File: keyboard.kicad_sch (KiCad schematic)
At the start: 8 parts, among them J3 KEYBOARD / USER FIT, J5 MODULE LINK / OPTIONAL, U8 PCF8574T

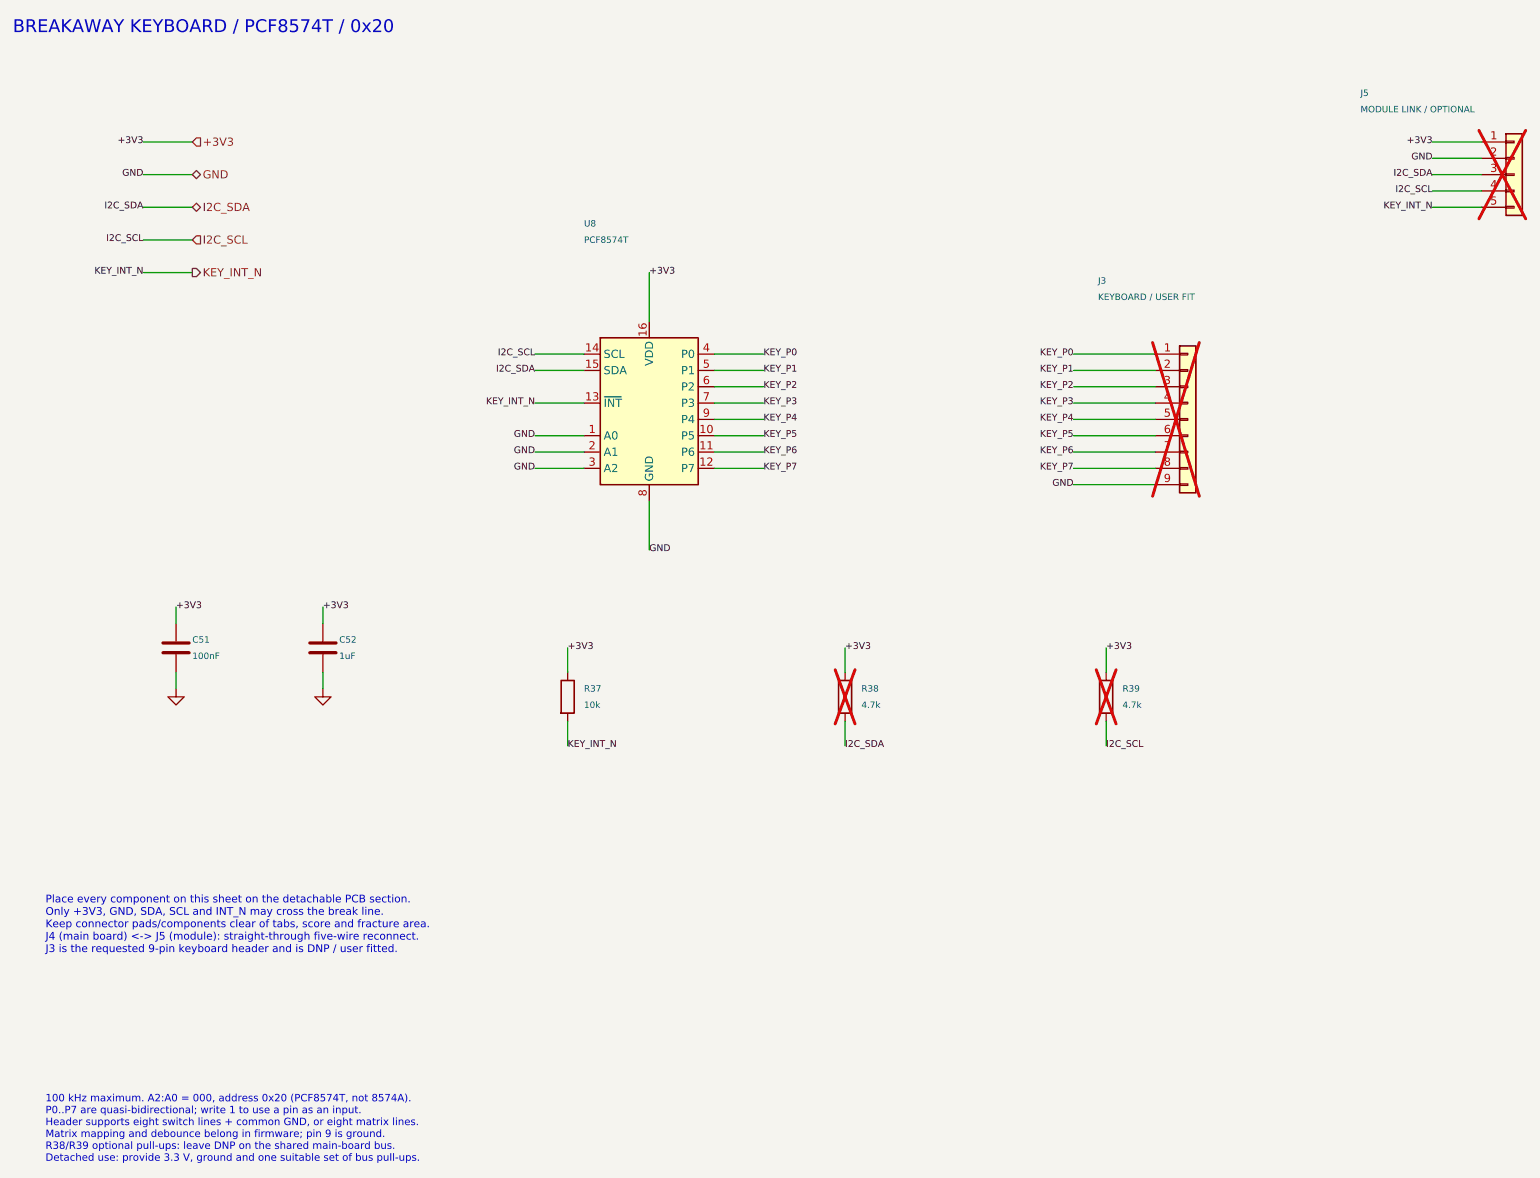
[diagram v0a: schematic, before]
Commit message: Keep keypad signals on center seven header pins
Retain the DNP nine-pin header with pins 1 and 9 isolated. Map pins 2-8
to PCF8574 P0-P6, preserving the early prototype's seven-contact order,
and leave P7 unconnected.

Document the researched keypad matrix mapping and scanning behavior.
Update schematic notes, connectivity checks, BOM, verification report,
and schematic PDF.

Validation: zero native KiCad ERC violations; seven-contact mapping
matches the early netlist; isolated pins and DNP status verified;
updated schematic pages visually inspected.
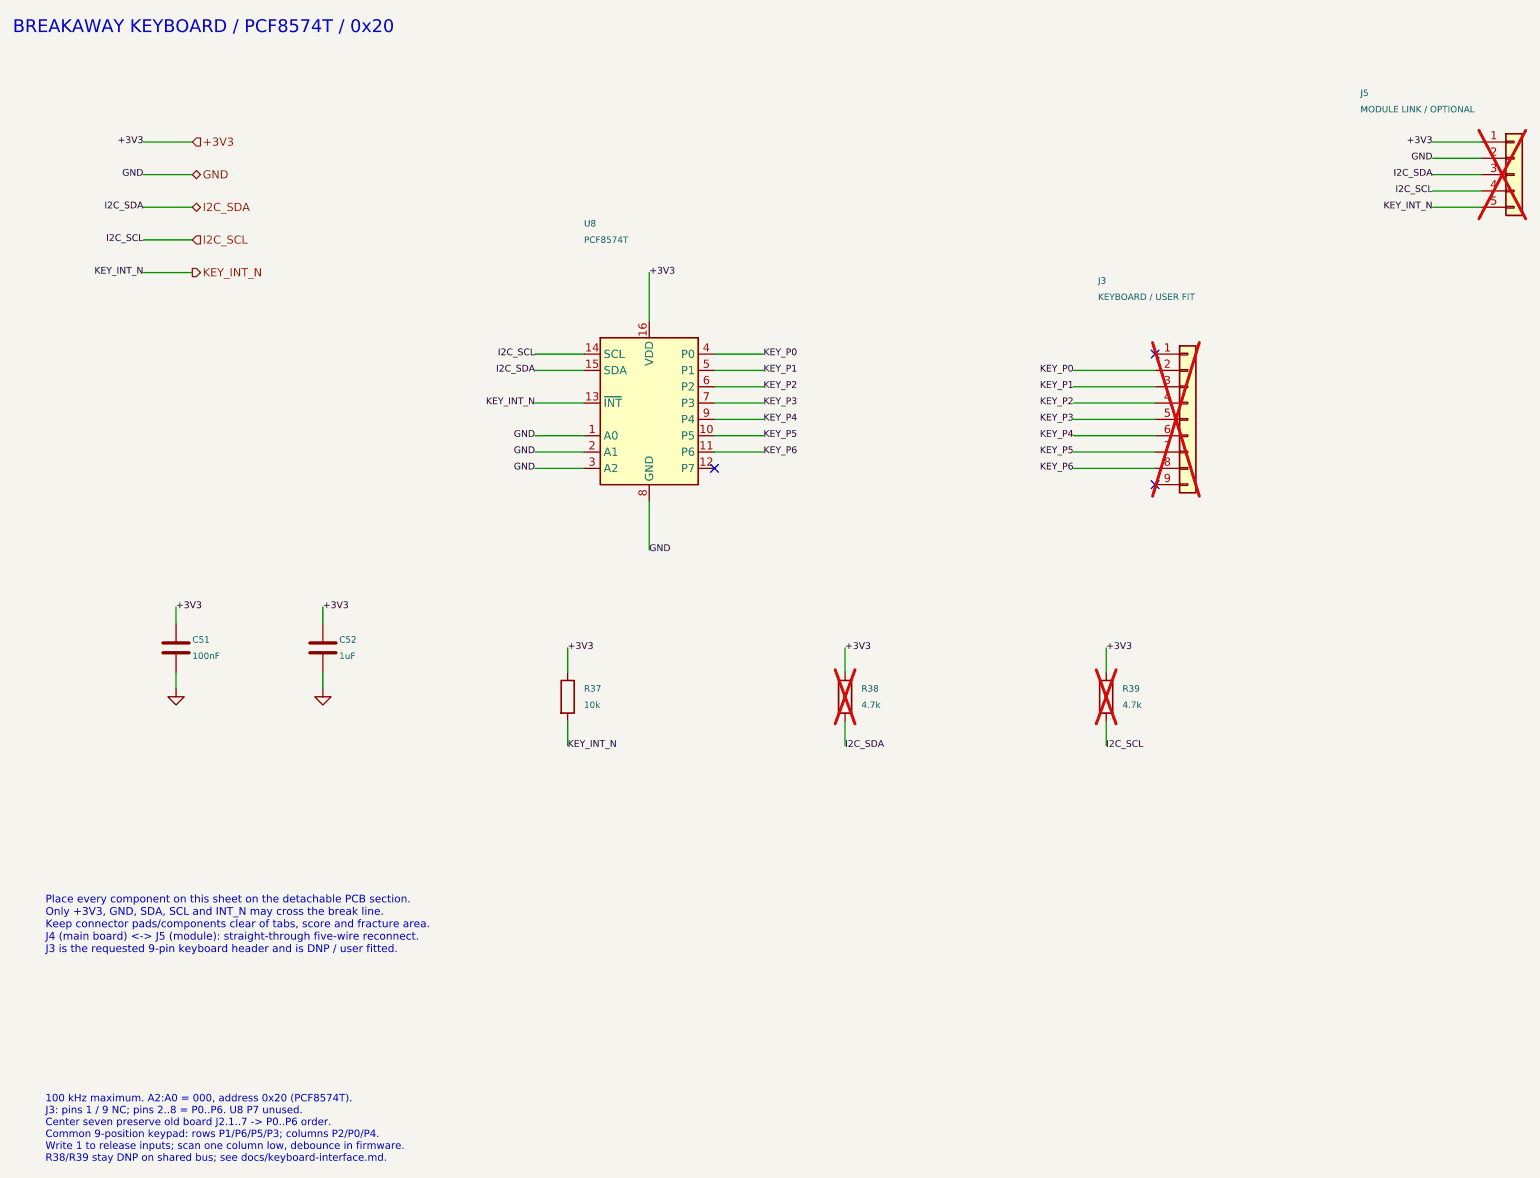
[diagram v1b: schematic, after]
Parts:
- J3: Compatibility (none) -> Center seven retain old nucula-board J2.1..7 -> PCF8574 P0.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; Keypad Reference (none) -> https://learn.adafruit.com/matrix-keypad/pinouts; Pinout 1..8=P0..P7; 9=GND -> 1=NC; 2..8=P0..P6; 9=NC; Status (none) -> DNP/user-fitted 9-pin header; pins 1 and 9 isolated; 3x4 ma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
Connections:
- net GND: no longer J3.9 (Pin_9)
- net KEY_P0: now also J3.2 (Pin_2); no longer J3.1 (Pin_1)
- net KEY_P1: now also J3.3 (Pin_3); no longer J3.2 (Pin_2)
- net KEY_P2: now also J3.4 (Pin_4); no longer J3.3 (Pin_3)
- net KEY_P3: now also J3.5 (Pin_5); no longer J3.4 (Pin_4)
- net KEY_P4: now also J3.6 (Pin_6); no longer J3.5 (Pin_5)
- net KEY_P5: now also J3.7 (Pin_7); no longer J3.6 (Pin_6)
- net KEY_P6: now also J3.8 (Pin_8); no longer J3.7 (Pin_7)
- net KEY_P7: no longer names the net of U8.12 (P7)
- net KEY_P7: no longer J3.8 (Pin_8)
- no-connect marks 0 -> 3
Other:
- note added: "100 kHz maximum. A2:A0 = 000, address 0x20 (PCF8574T). J3: pins 1 / 9 NC; pins 2..8 = P0..P6. U8 P7 unused. Center seven preserve old board J2.1..7 -> P0..P6 order. Common 9-position keypad: rows P1/P6/P5/P3; columns P2/P0/P4. Write 1 to release inputs; scan one column low, debounce in firmware. R38/R39 stay DNP on shared bus; see docs/keyboard-interface.md."
- note removed: "100 kHz maximum. A2:A0 = 000, address 0x20 (PCF8574T, not 8574A). P0..P7 are quasi-bidirectional; write 1 to use a pin as an input. Header supports eight switch lines + common GND, or eight matrix lines. Matrix mapping and debounce belong in firmware; pin 9 is ground. R38/R39 optional pull-ups: leave DNP on the shared main-board bus. Detached use: provide 3.3 V, ground and one suitable set of bus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"
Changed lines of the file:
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@@
-    )
-  )
-  (wire
-    (pts
-      (xy 124.46 86.36)
-      (xy 132.08 86.36)
-    )
-    (stroke
-      (width 0)
-      (type default)
-    )
-  )
-  (label "KEY_P7"
-    (at 132.08 86.36 0)
-    (effects
-      (font
-        (size 1.05 1.05)
-      )
-      (justify left)
     )
   )
@@
       )
     )
-    (property "Pinout" "1..8=P0..P7; 9=GND"
+    (property "Pinout" "1=NC; 2..8=P0..P6; 9=NC"
       (at 198.12 78.74 0)
       (effects
@@
         (hide yes)
         (justify left)
+      )
+    )
+    (property "Compatibility" "Center seven retain old nucula-board J2.1..7 -> PCF8574 P0..P6 order"
+      (at 198.12 78.74 0)
+      (effects
+        (font
+          (size 1.27 1.27)
+        )
+        (hide yes)
+      )
+    )
+    (property "Keypad Reference" "https://learn.adafruit.com/matrix-keypad/pinouts"
+      (at 198.12 78.74 0)
+      (effects
+        (font
+          (size 1.27 1.27)
+        )
+        (hide yes)
+      )
+    )
+    (property "Status" "DNP/user-fitted 9-pin header; pins 1 and 9 isolated; 3x4 matrix on center seven"
+      (at 198.12 78.74 0)
+      (effects
+        (font
+          (size 1.27 1.27)
+        )
+        (hide yes)
       )
     )
@@
   (wire
     (pts
-      (xy 193.04 68.58)
-      (xy 180.34 68.58)
-    )
-    (stroke
-      (width 0)
-      (type default)
-    )
-  )
-  (label "KEY_P0"
-    (at 180.34 68.58 180)
-    (effects
-      (font
-        (size 1.05 1.05)
-      )
-      (justify right)
-    )
-  )
-  (wire
-    (pts
       (xy 193.04 71.12)
       (xy 180.34 71.12)
@@
     )
   )
-  (label "KEY_P1"
+  (label "KEY_P0"
     (at 180.34 71.12 180)
     (effects
@@
     )
   )
-  (label "KEY_P2"
+  (label "KEY_P1"
     (at 180.34 73.66 180)
     (effects
@@
     )
   )
-  (label "KEY_P3"
+  (label "KEY_P2"
     (at 180.34 76.2 180)
     (effects
@@
     )
   )
-  (label "KEY_P4"
+  (label "KEY_P3"
     (at 180.34 78.74 180)
     (effects
@@
     )
   )
-  (label "KEY_P5"
+  (label "KEY_P4"
     (at 180.34 81.28 180)
     (effects
@@
     )
   )
-  (label "KEY_P6"
+  (label "KEY_P5"
     (at 180.34 83.82 180)
     (effects
@@
     )
   )
-  (label "KEY_P7"
+  (label "KEY_P6"
     (at 180.34 86.36 180)
-    (effects
-      (font
-        (size 1.05 1.05)
-      )
-      (justify right)
-    )
-  )
-  (wire
-    (pts
-      (xy 193.04 88.9)
-      (xy 180.34 88.9)
-    )
-    (stroke
-      (width 0)
-      (type default)
-    )
-  )
-  (label "GND"
-    (at 180.34 88.9 180)
     (effects
       (font
@@
     )
   )
-  (text "100 kHz maximum. A2:A0 = 000, address 0x20 (PCF8574T, not 8574A).\nP0..P7 are quasi-bidirectional; write 1 to use a pin as an input.\nHeader supports eight switch lines + common GND, or eight matrix lines.\nMatrix mapping and debounce belong in firmware; pin 9 is ground.\nR38/R39 optional pull-ups: leave DNP on the shared main-board bus.\nDetached use: provide 3.3 V, ground and one suitable set of bus pull-ups."
+  (text "100 kHz maximum. A2:A0 = 000, address 0x20 (PCF8574T).\nJ3: pins 1 / 9 NC; pins 2..8 = P0..P6. U8 P7 unused.\nCenter seven preserve old board J2.1..7 -> P0..P6 order.\nCommon 9-position keypad: rows P1/P6/P5/P3; columns P2/P0/P4.\nWrite 1 to release inputs; scan one column low, debounce in firmware.\nR38/R39 stay DNP on shared bus; see docs/keyboard-interface.md."
     (at 20.32 189.23 0)
     (effects
@@
   )
   (embedded_fonts no)
+  (no_connect
+    (at 193.04 68.58)
+  )
+  (no_connect
+    (at 193.04 88.9)
+  )
+  (no_connect
+    (at 124.46 86.36)
+  )
 )

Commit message: Prepare components and JLCPCB BOM for 10-board assembly
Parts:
- C51: LCSC (none) -> C1591; MPN (none) -> CL10B104KB8NNNC; Manufacturer (none) -> Samsung Electro-Mechanics; Voltage 10 V -> 50 V
- C52: LCSC (none) -> C28323; MPN (none) -> CL21B105KBFNNNE; Manufacturer (none) -> Samsung Electro-Mechanics; Tolerance 20% -> 10%; Voltage 10 V -> 50 V
- R37: LCSC (none) -> C25804; MPN (none) -> 0603WAF1002T5E; Manufacturer (none) -> UNI-ROYAL(Uniroyal Elec)
- U8: LCSC (none) -> C7605; Manufacturer NXP -> NXP Semicon
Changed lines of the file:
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@@
       )
     )
-    (property "Manufacturer" "NXP"
+    (property "Manufacturer" "NXP Semicon"
       (at 114.3 78.74 0)
       (effects
@@
           (unit 1)
         )
+      )
+    )
+    (property "LCSC" "C7605"
+      (at 114.3 78.74 0)
+      (effects
+        (font
+          (size 1.0 1.0)
+        )
+        (hide yes)
       )
     )
@@
       )
     )
-    (property "Datasheet" ""
+    (property "Datasheet" "https://www.lcsc.com/datasheet/lcsc_datasheet_2304140030_Samsung-Electro-Mechanics-CL10B104KB8NNNC_C1591.pdf"
       (at 40.64 114.3 0)
       (effects
@@
       )
     )
-    (property "Voltage" "10 V"
+    (property "Voltage" "50 V"
       (at 40.64 114.3 0)
       (effects
@@
           (unit 1)
         )
+      )
+    )
+    (property "Manufacturer" "Samsung Electro-Mechanics"
+      (at 40.64 114.3 0)
+      (effects
+        (font
+          (size 1.0 1.0)
+        )
+        (hide yes)
+      )
+    )
+    (property "MPN" "CL10B104KB8NNNC"
+      (at 40.64 114.3 0)
+      (effects
+        (font
+          (size 1.0 1.0)
+        )
+        (hide yes)
+      )
+    )
+    (property "LCSC" "C1591"
+      (at 40.64 114.3 0)
+      (effects
+        (font
+          (size 1.0 1.0)
+        )
+        (hide yes)
       )
     )
@@
       )
     )
-    (property "Datasheet" ""
+    (property "Datasheet" "https://www.lcsc.com/datasheet/lcsc_datasheet_2304140030_Samsung-Electro-Mechanics-CL21B105KBFNNNE_C28323.pdf"
       (at 63.5 114.3 0)
       (effects
@@
       )
     )
-    (property "Voltage" "10 V"
+    (property "Voltage" "50 V"
       (at 63.5 114.3 0)
       (effects
@@
       )
     )
-    (property "Tolerance" "20%"
+    (property "Tolerance" "10%"
       (at 63.5 114.3 0)
       (effects
@@
           (unit 1)
         )
+      )
+    )
+    (property "Manufacturer" "Samsung Electro-Mechanics"
+      (at 63.5 114.3 0)
+      (effects
+        (font
+          (size 1.0 1.0)
+        )
+        (hide yes)
+      )
+    )
+    (property "MPN" "CL21B105KBFNNNE"
+      (at 63.5 114.3 0)
+      (effects
+        (font
+          (size 1.0 1.0)
+        )
+        (hide yes)
+      )
+    )
+    (property "LCSC" "C28323"
+      (at 63.5 114.3 0)
+      (effects
+        (font
+          (size 1.0 1.0)
+        )
+        (hide yes)
       )
     )
@@
       )
     )
-    (property "Datasheet" ""
+    (property "Datasheet" "https://www.lcsc.com/datasheet/lcsc_datasheet_2206010045_UNI-ROYAL-Uniroyal-Elec-0603WAF1002T5E_C25804.pdf"
       (at 101.6 121.92 0)
       (effects
@@
       )
     )
+    (property "Manufacturer" "UNI-ROYAL(Uniroyal Elec)"
+      (at 101.6 121.92 0)
+      (effects
+        (font
+          (size 1.0 1.0)
+        )
+        (hide yes)
+      )
+    )
+    (property "MPN" "0603WAF1002T5E"
+      (at 101.6 121.92 0)
+      (effects
+        (font
+          (size 1.0 1.0)
+        )
+        (hide yes)
+      )
+    )
+    (property "LCSC" "C25804"
+      (at 101.6 121.92 0)
+      (effects
+        (font
+          (size 1.0 1.0)
+        )
+        (hide yes)
+      )
+    )

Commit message: Qualify stocked parts and release October 9 production package
Replace four unavailable BOM lines, preserve rev-A NFC copper and placement, and include 792 simulation cases with fresh production validation. Remove superseded manufacturing packages so only the latest release remains.
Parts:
- C51: LCSC C1591 -> C913912; MPN CL10B104KB8NNNC -> CL10B104KB8NNNL
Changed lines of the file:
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@@
       )
     )
-    (property "Datasheet" "https://www.lcsc.com/datasheet/lcsc_datasheet_2304140030_Samsung-Electro-Mechanics-CL10B104KB8NNNC_C1591.pdf"
+    (property "Datasheet" "https://product.samsungsem.com/cn/mlcc/CL10B104KB8NNN.do"
       (at 40.64 114.3 0)
       (effects
@@
       )
     )
-    (property "MPN" "CL10B104KB8NNNC"
+    (property "MPN" "CL10B104KB8NNNL"
       (at 40.64 114.3 0)
       (effects
@@
       )
     )
-    (property "LCSC" "C1591"
+    (property "LCSC" "C913912"
       (at 40.64 114.3 0)
       (effects
